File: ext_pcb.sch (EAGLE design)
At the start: 38 parts, among them CN10 MCV_05/4-G-2,5V, CN11 MCV_05/4-G-2,5V, CN12 MCV_05/4-G-2,5V, CN13 MCV_05/4-G-2,5V, CN15 MCV_05/2-G-2,5V, CN16 MCV_05/2-G-2,5V, CN17 MCV_05/2-G-2,5V, CN2 53047-08, CN3 53047-06, CN4 MCV_05/4-G-2,5V, CN5 53047-04, CN6 MCV_05/4-G-2,5V, CN7 MCV_05/4-G-2,5V, CN8 MCV_05/4-G-2,5V, CN9 MCV_05/6-G-2,5V, U1 LP298XS, U2 4049D

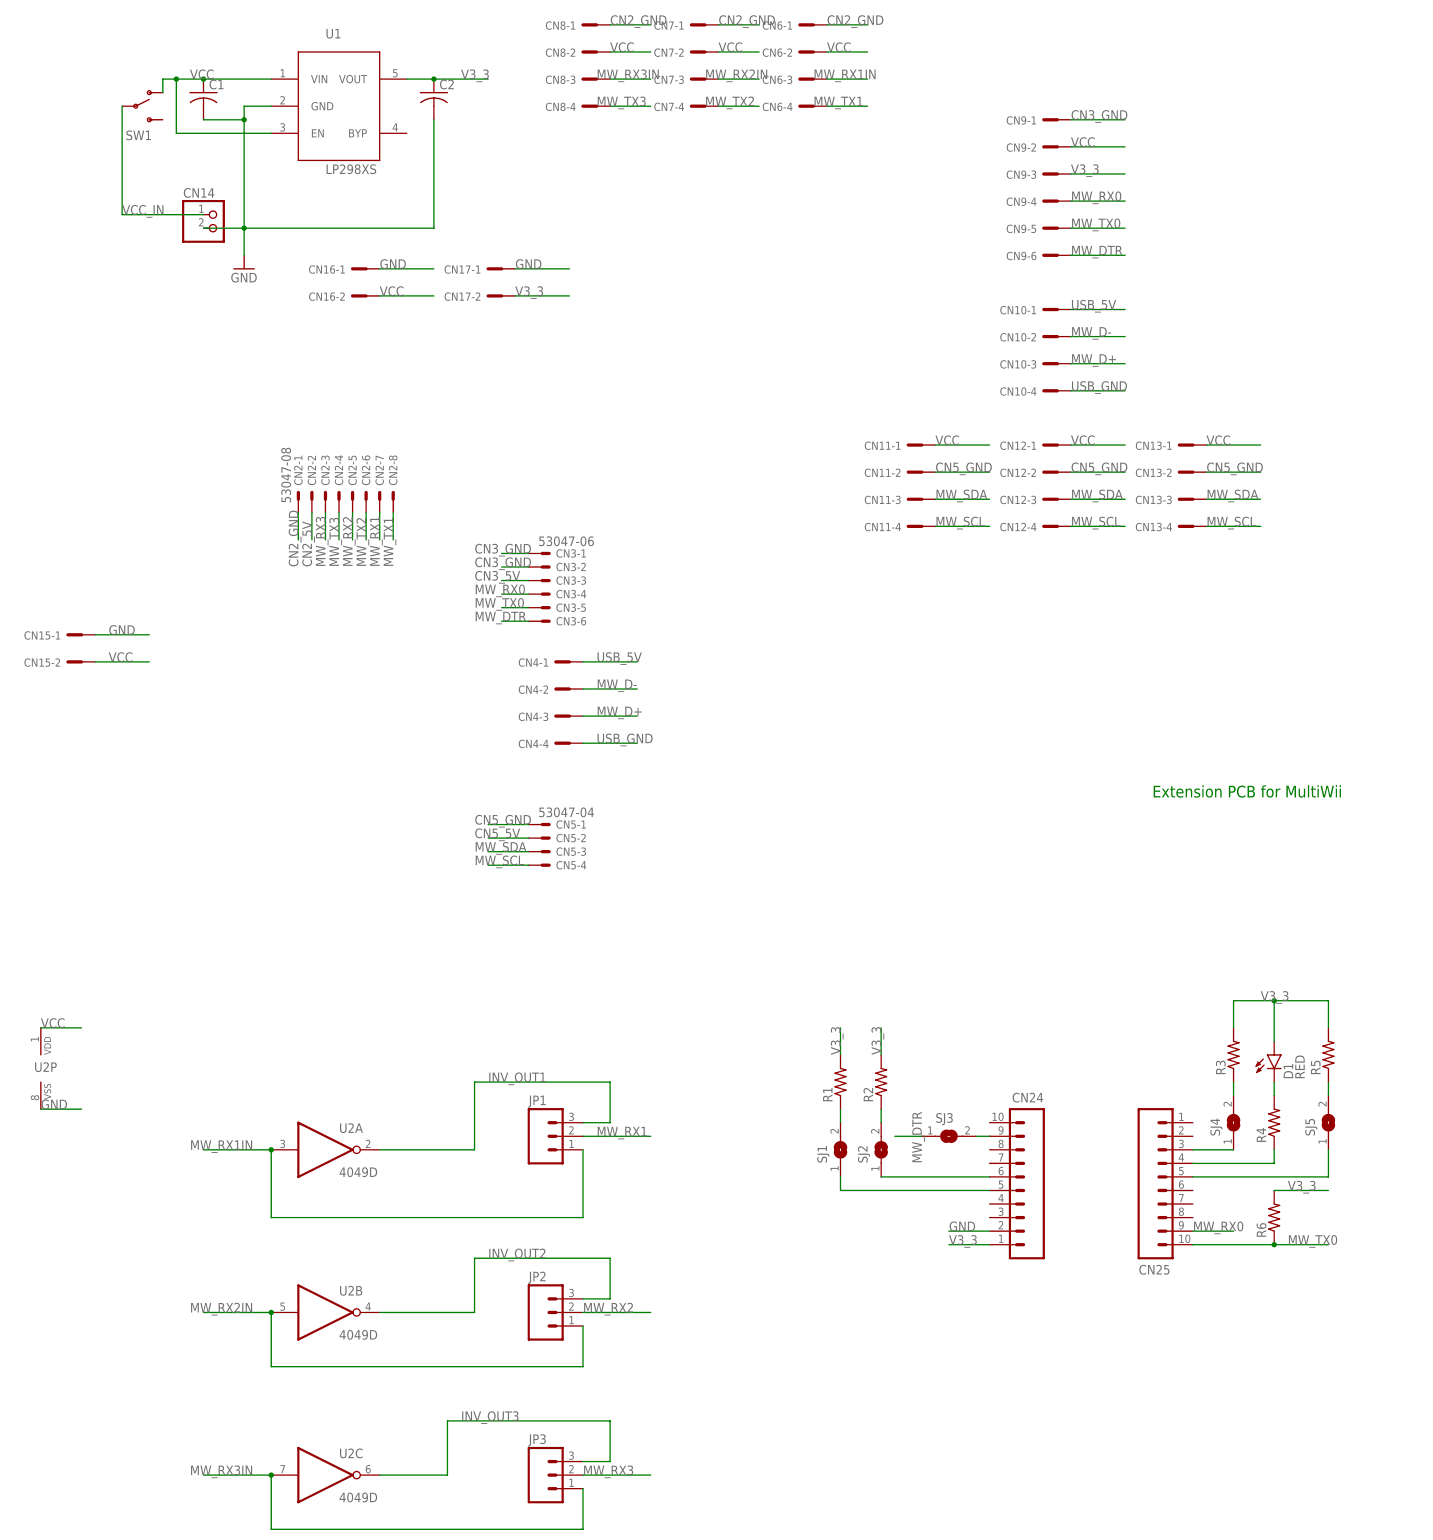
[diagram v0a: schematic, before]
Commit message: Change ground connections
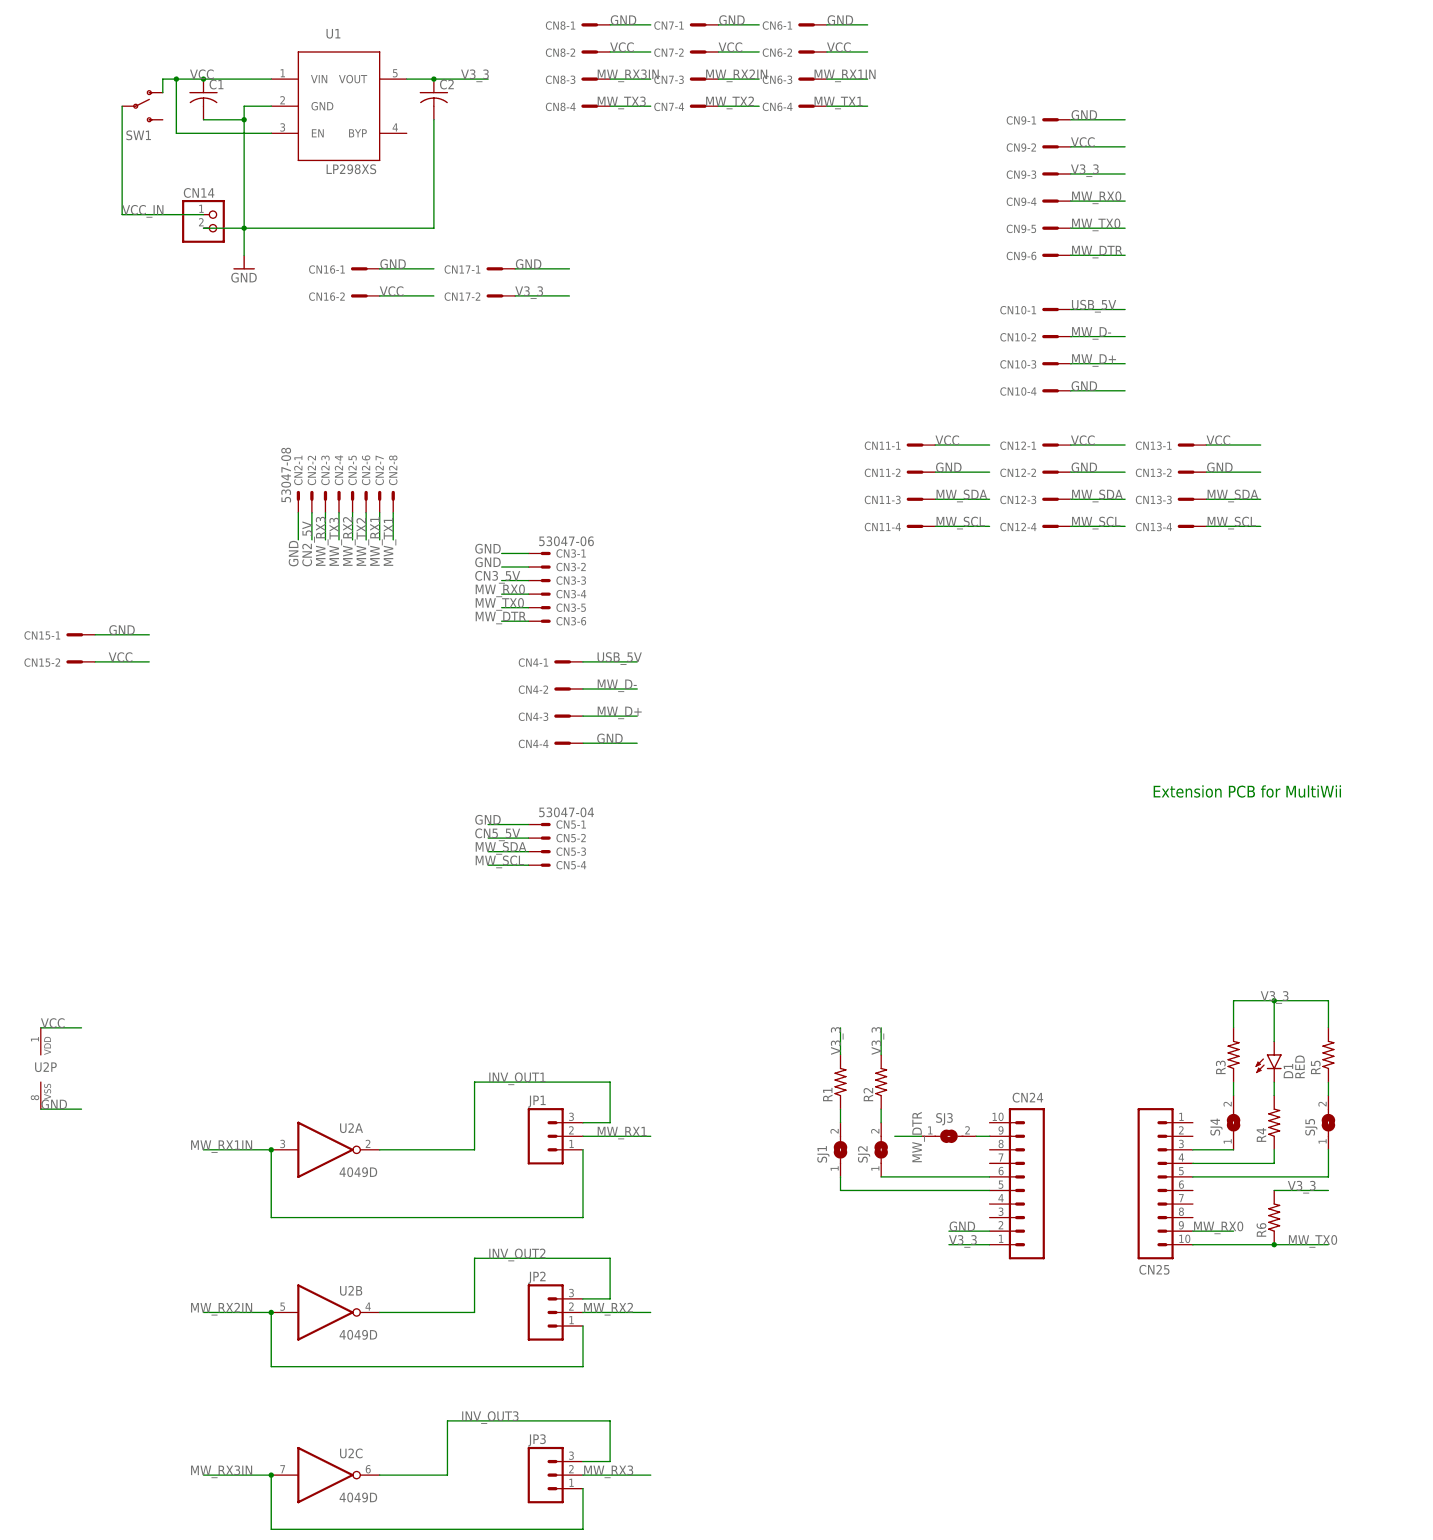
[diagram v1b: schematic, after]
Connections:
- removed net CN2_GND: CN2-1.S, CN6-1.SK, CN7-1.SK, CN8-1.SK
- removed net CN3_GND: CN3-1.S, CN3-2.S, CN9-1.SK
- removed net CN5_GND: CN11-2.SK, CN12-2.SK, CN13-2.SK, CN5-1.S
- removed net USB_GND: CN10-4.SK, CN4-4.SK
- net GND: now also CN10-4.SK, CN11-2.SK, CN12-2.SK, CN13-2.SK, CN2-1.S, CN3-1.S, CN3-2.S, CN4-4.SK, CN5-1.S, CN6-1.SK, CN7-1.SK, CN8-1.SK, CN9-1.SK
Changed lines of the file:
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@@
 <?xml version="1.0" encoding="utf-8"?>
 <!DOCTYPE eagle SYSTEM "eagle.dtd">
-<eagle version="7.2.0">
+<eagle version="7.4.0">
 <drawing>
 <settings>
@@
 <label x="177.8" y="-60.96" size="1.778" layer="95"/>
 </segment>
+<segment>
+<pinref part="CN4" gate="-4" pin="SK"/>
+<wire x1="109.22" y1="30.48" x2="119.38" y2="30.48" width="0.1524" layer="91"/>
+<label x="111.76" y="30.48" size="1.778" layer="95"/>
+</segment>
+<segment>
+<pinref part="CN10" gate="-4" pin="SK"/>
+<wire x1="200.66" y1="96.52" x2="210.82" y2="96.52" width="0.1524" layer="91"/>
+<label x="200.66" y="96.52" size="1.778" layer="95"/>
+</segment>
+<segment>
+<pinref part="CN5" gate="-1" pin="S"/>
+<wire x1="99.06" y1="15.24" x2="91.44" y2="15.24" width="0.1524" layer="91"/>
+<label x="88.9" y="15.24" size="1.778" layer="95"/>
+</segment>
+<segment>
+<pinref part="CN11" gate="-2" pin="SK"/>
+<wire x1="175.26" y1="81.28" x2="185.42" y2="81.28" width="0.1524" layer="91"/>
+<label x="175.26" y="81.28" size="1.778" layer="95"/>
+</segment>
+<segment>
+<pinref part="CN12" gate="-2" pin="SK"/>
+<wire x1="200.66" y1="81.28" x2="210.82" y2="81.28" width="0.1524" layer="91"/>
+<label x="200.66" y="81.28" size="1.778" layer="95"/>
+</segment>
+<segment>
+<pinref part="CN13" gate="-2" pin="SK"/>
+<wire x1="226.06" y1="81.28" x2="236.22" y2="81.28" width="0.1524" layer="91"/>
+<label x="226.06" y="81.28" size="1.778" layer="95"/>
+</segment>
+<segment>
+<pinref part="CN2" gate="-1" pin="S"/>
+<wire x1="55.88" y1="73.66" x2="55.88" y2="68.58" width="0.1524" layer="91"/>
+<label x="55.88" y="63.5" size="1.778" layer="95" rot="R90"/>
+</segment>
+<segment>
+<pinref part="CN8" gate="-1" pin="SK"/>
+<wire x1="114.3" y1="165.1" x2="121.92" y2="165.1" width="0.1524" layer="91"/>
+<label x="114.3" y="165.1" size="1.778" layer="95"/>
+</segment>
+<segment>
+<pinref part="CN7" gate="-1" pin="SK"/>
+<wire x1="134.62" y1="165.1" x2="142.24" y2="165.1" width="0.1524" layer="91"/>
+<label x="134.62" y="165.1" size="1.778" layer="95"/>
+</segment>
+<segment>
+<pinref part="CN6" gate="-1" pin="SK"/>
+<wire x1="154.94" y1="165.1" x2="162.56" y2="165.1" width="0.1524" layer="91"/>
+<label x="154.94" y="165.1" size="1.778" layer="95"/>
+</segment>
+<segment>
+<pinref part="CN3" gate="-1" pin="S"/>
+<wire x1="99.06" y1="66.04" x2="93.98" y2="66.04" width="0.1524" layer="91"/>
+<label x="88.9" y="66.04" size="1.778" layer="95"/>
+</segment>
+<segment>
+<pinref part="CN3" gate="-2" pin="S"/>
+<wire x1="99.06" y1="63.5" x2="93.98" y2="63.5" width="0.1524" layer="91"/>
+<label x="88.9" y="63.5" size="1.778" layer="95"/>
+</segment>
+<segment>
+<pinref part="CN9" gate="-1" pin="SK"/>
+<wire x1="200.66" y1="147.32" x2="210.82" y2="147.32" width="0.1524" layer="91"/>
+<label x="200.66" y="147.32" size="1.778" layer="95"/>
+</segment>
 </net>
 <net name="MW_RX3" class="0">
@@
 </segment>
 </net>
-<net name="CN2_GND" class="0">
-<segment>
-<pinref part="CN2" gate="-1" pin="S"/>
-<wire x1="55.88" y1="73.66" x2="55.88" y2="68.58" width="0.1524" layer="91"/>
-<label x="55.88" y="63.5" size="1.778" layer="95" rot="R90"/>
-</segment>
-<segment>
-<pinref part="CN8" gate="-1" pin="SK"/>
-<wire x1="114.3" y1="165.1" x2="121.92" y2="165.1" width="0.1524" layer="91"/>
-<label x="114.3" y="165.1" size="1.778" layer="95"/>
-</segment>
-<segment>
-<pinref part="CN7" gate="-1" pin="SK"/>
-<wire x1="134.62" y1="165.1" x2="142.24" y2="165.1" width="0.1524" layer="91"/>
-<label x="134.62" y="165.1" size="1.778" layer="95"/>
-</segment>
-<segment>
-<pinref part="CN6" gate="-1" pin="SK"/>
-<wire x1="154.94" y1="165.1" x2="162.56" y2="165.1" width="0.1524" layer="91"/>
-<label x="154.94" y="165.1" size="1.778" layer="95"/>
-</segment>
-</net>
-<net name="CN3_GND" class="0">
-<segment>
-<pinref part="CN3" gate="-1" pin="S"/>
-<wire x1="99.06" y1="66.04" x2="93.98" y2="66.04" width="0.1524" layer="91"/>
-<label x="88.9" y="66.04" size="1.778" layer="95"/>
-</segment>
-<segment>
-<pinref part="CN3" gate="-2" pin="S"/>
-<wire x1="99.06" y1="63.5" x2="93.98" y2="63.5" width="0.1524" layer="91"/>
-<label x="88.9" y="63.5" size="1.778" layer="95"/>
-</segment>
-<segment>
-<pinref part="CN9" gate="-1" pin="SK"/>
-<wire x1="200.66" y1="147.32" x2="210.82" y2="147.32" width="0.1524" layer="91"/>
-<label x="200.66" y="147.32" size="1.778" layer="95"/>
-</segment>
-</net>
-<net name="USB_GND" class="0">
-<segment>
-<pinref part="CN4" gate="-4" pin="SK"/>
-<wire x1="109.22" y1="30.48" x2="119.38" y2="30.48" width="0.1524" layer="91"/>
-<label x="111.76" y="30.48" size="1.778" layer="95"/>
-</segment>
-<segment>
-<pinref part="CN10" gate="-4" pin="SK"/>
-<wire x1="200.66" y1="96.52" x2="210.82" y2="96.52" width="0.1524" layer="91"/>
-<label x="200.66" y="96.52" size="1.778" layer="95"/>
-</segment>
-</net>
-<net name="CN5_GND" class="0">
-<segment>
-<pinref part="CN5" gate="-1" pin="S"/>
-<wire x1="99.06" y1="15.24" x2="91.44" y2="15.24" width="0.1524" layer="91"/>
-<label x="88.9" y="15.24" size="1.778" layer="95"/>
-</segment>
-<segment>
-<pinref part="CN11" gate="-2" pin="SK"/>
-<wire x1="175.26" y1="81.28" x2="185.42" y2="81.28" width="0.1524" layer="91"/>
-<label x="175.26" y="81.28" size="1.778" layer="95"/>
-</segment>
-<segment>
-<pinref part="CN12" gate="-2" pin="SK"/>
-<wire x1="200.66" y1="81.28" x2="210.82" y2="81.28" width="0.1524" layer="91"/>
-<label x="200.66" y="81.28" size="1.778" layer="95"/>
-</segment>
-<segment>
-<pinref part="CN13" gate="-2" pin="SK"/>
-<wire x1="226.06" y1="81.28" x2="236.22" y2="81.28" width="0.1524" layer="91"/>
-<label x="226.06" y="81.28" size="1.778" layer="95"/>
-</segment>
-</net>
